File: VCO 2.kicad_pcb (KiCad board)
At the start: 2 copper layers, 182.4 x 128.6 mm, 0 parts

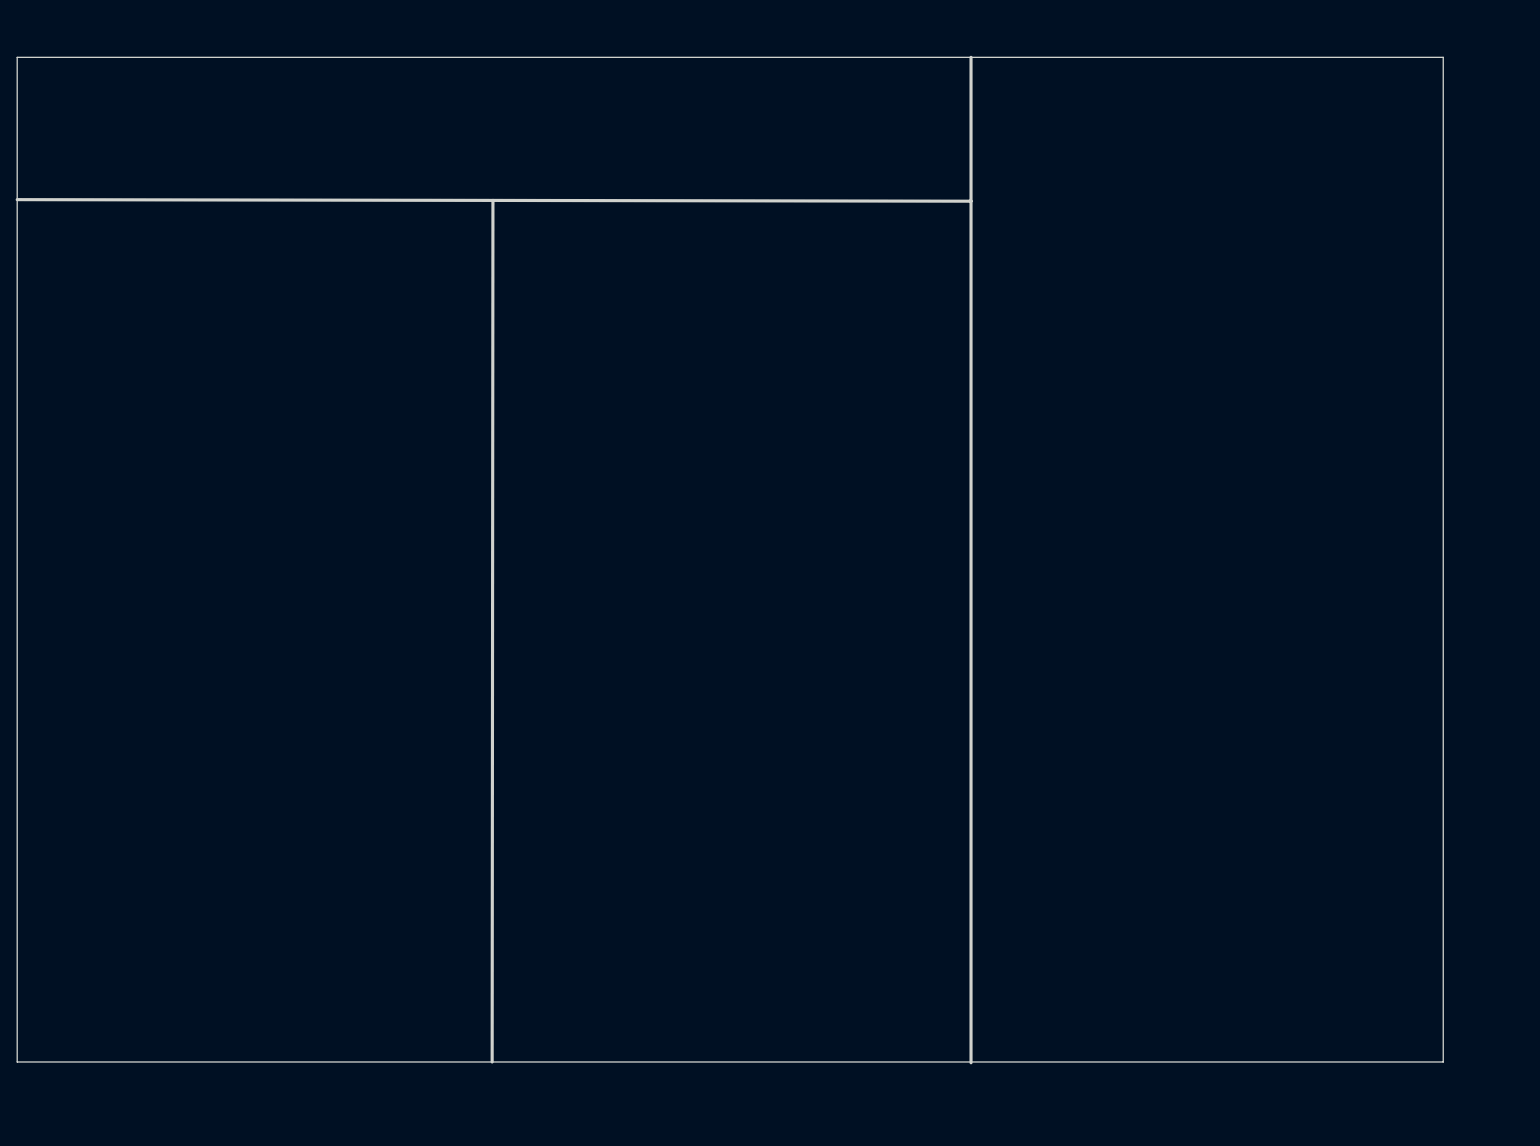
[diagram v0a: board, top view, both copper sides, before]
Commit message: Designed PCB and generated JLCPCB files
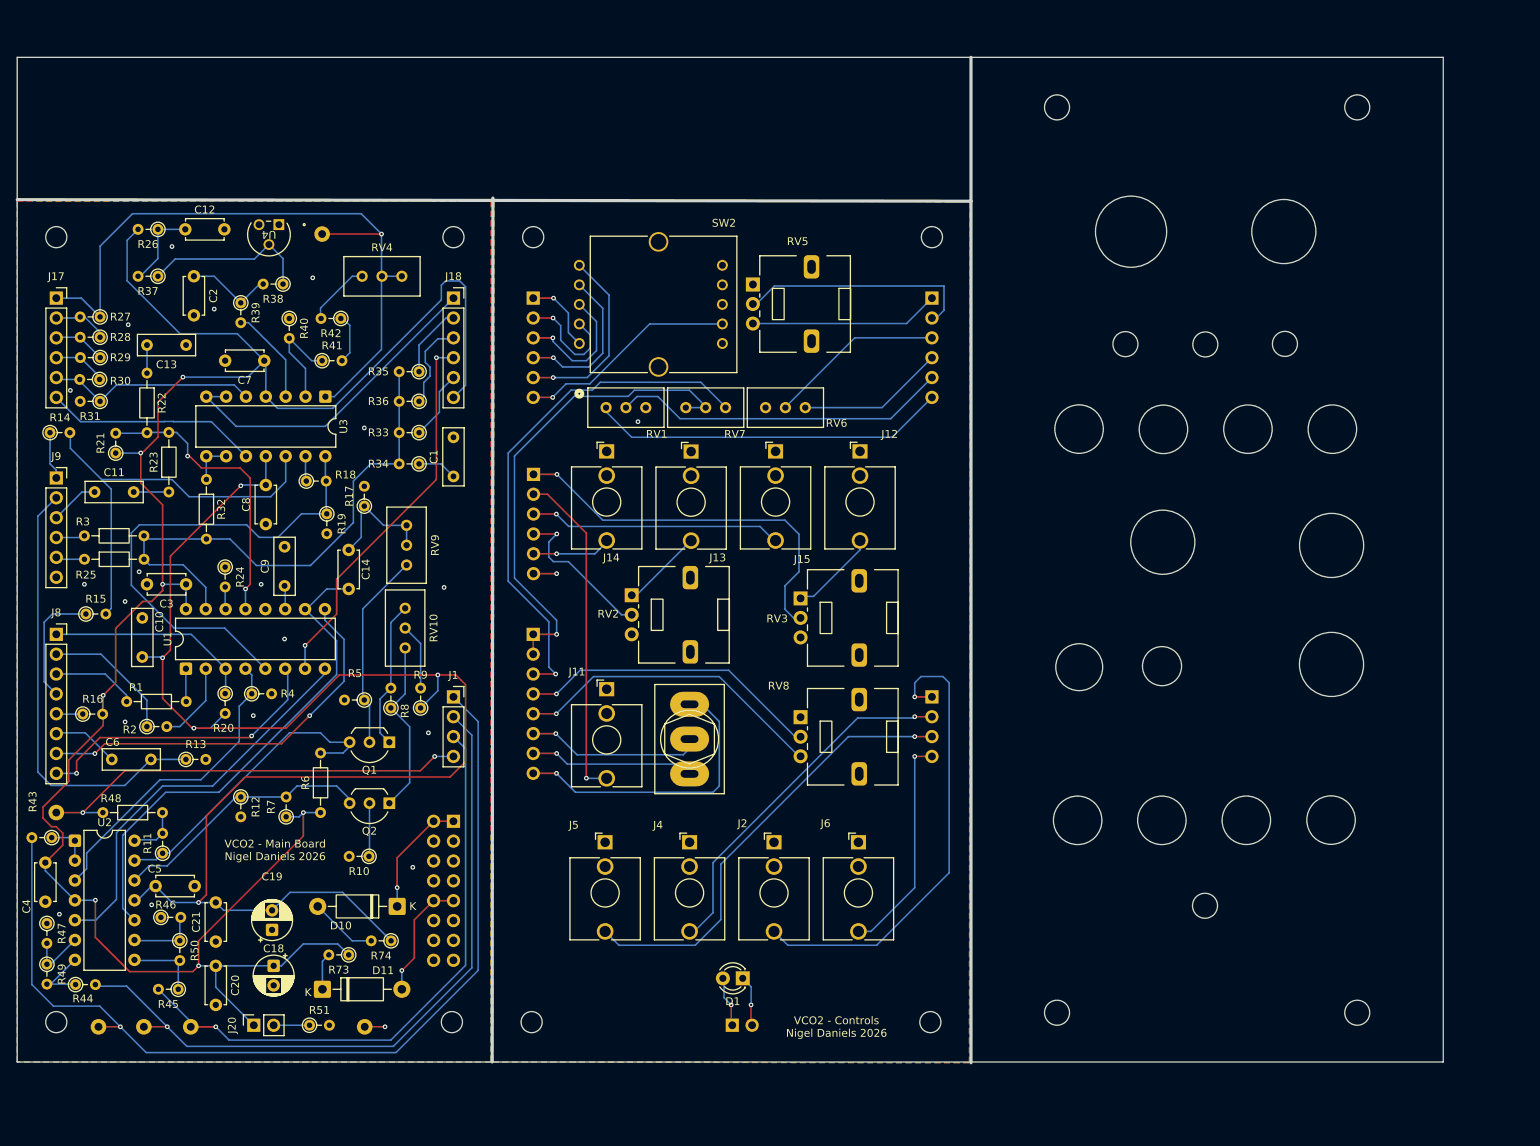
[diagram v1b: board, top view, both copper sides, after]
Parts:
- added C1: 10nF f, Capacitor_THT:C_Rect_L7.2mm_W2.5mm_P5.00mm, F.Cu at (75.8, 73.6)
- added C10: 100nF f, Capacitor_THT:C_Rect_L7.2mm_W2.5mm_P5.00mm, F.Cu at (36.0, 91.7)
- added C11: 100nF f, Capacitor_THT:C_Rect_L7.2mm_W2.5mm_P5.00mm, F.Cu at (29.9, 75.6)
- added C12: 0.1μF c, Capacitor_THT:C_Disc_D4.7mm_W2.5mm_P5.00mm, F.Cu at (41.5, 42.0)
- added C13: 1nF f, Capacitor_THT:C_Rect_L7.2mm_W2.5mm_P5.00mm, F.Cu at (41.6, 56.8)
- added C14: 10uF c, Capacitor_THT:C_Disc_D4.7mm_W2.5mm_P5.00mm, F.Cu at (62.4, 83.0)
- added C18: 47μF e, Capacitor_THT:CP_Radial_D5.0mm_P2.50mm, F.Cu at (52.8, 136.2)
- added C19: 47μF e, Capacitor_THT:CP_Radial_D5.0mm_P2.50mm, F.Cu at (52.6, 131.6)
- added C2: 10μF c, Capacitor_THT:C_Disc_D4.7mm_W2.5mm_P5.00mm, F.Cu at (42.6, 48.0)
- added C20: 0.1μF c, Capacitor_THT:C_Disc_D4.7mm_W2.5mm_P5.00mm, F.Cu at (45.4, 136.2)
- added C21: 0.1μF c, Capacitor_THT:C_Disc_D4.7mm_W2.5mm_P5.00mm, F.Cu at (45.4, 133.1)
- added C3: 100nF c, Capacitor_THT:C_Disc_D4.7mm_W2.5mm_P5.00mm, F.Cu at (41.6, 87.4)
- added C4: 0.1μF c, Capacitor_THT:C_Disc_D4.7mm_W2.5mm_P5.00mm, F.Cu at (23.6, 123.0)
- added C5: 0.1μF c, Capacitor_THT:C_Disc_D4.7mm_W2.5mm_P5.00mm, F.Cu at (42.7, 126.0)
- added C6: 1000pF f, Capacitor_THT:C_Rect_L7.2mm_W2.5mm_P5.00mm, F.Cu at (32.1, 109.8)
- added C7: 0.1μF c, Capacitor_THT:C_Disc_D4.7mm_W2.5mm_P5.00mm, F.Cu at (51.6, 58.8)
- added C8: 0.1μF c, Capacitor_THT:C_Disc_D4.7mm_W2.5mm_P5.00mm, F.Cu at (51.8, 79.7)
- added C9: 1nF f, Capacitor_THT:C_Rect_L7.2mm_W2.5mm_P5.00mm, F.Cu at (54.2, 87.6)
- added D1: LED, LED_THT:LED_D3.0mm_FlatTop, F.Cu at (112.8, 137.8)
- added D10: 1N5819, Diode_THT:D_DO-41_SOD81_P10.16mm_Horizontal, F.Cu at (68.6, 128.6)
- added D11: 1N5819, Diode_THT:D_DO-41_SOD81_P10.16mm_Horizontal, F.Cu at (59.0, 139.2)
- added H1: ~, MountingHole:MountingHole_2.7mm_M2.5, F.Cu at (25.0, 43.0)
- added H10: ~, MountingHole:MountingHole_3.2mm_M3, F.Cu at (191.4, 26.4)
- added H11: ~, MountingHole:MountingHole_3.2mm_M3, F.Cu at (191.4, 142.2)
- added H12: ~, MountingHole:MountingHole_3.2mm_M3, F.Cu at (153.0, 142.2)
- added H2: ~, MountingHole:MountingHole_2.7mm_M2.5, F.Cu at (75.8, 43.0)
- added H3: ~, MountingHole:MountingHole_2.7mm_M2.5, F.Cu at (25.0, 143.4)
- added H4: ~, MountingHole:MountingHole_2.7mm_M2.5, F.Cu at (75.6, 143.4)
- added H5: ~, MountingHole:MountingHole_2.7mm_M2.5, F.Cu at (86.0, 43.0)
- added H6: ~, MountingHole:MountingHole_2.7mm_M2.5, F.Cu at (137.0, 43.0)
- added H7: ~, MountingHole:MountingHole_2.7mm_M2.5, F.Cu at (136.8, 143.4)
- added H8: ~, MountingHole:MountingHole_2.7mm_M2.5, F.Cu at (85.8, 143.4)
- added H9: ~, MountingHole:MountingHole_3.2mm_M3, F.Cu at (153.0, 26.4)
- added J1: OUT 1x4s, Connector_PinSocket_2.54mm:PinSocket_1x04_P2.54mm_Vertical, F.Cu at (75.8, 101.8)
- added J10: IN 1x6h, Connector_PinHeader_2.54mm:PinHeader_1x06_P2.54mm_Vertical, B.Cu at (86.0, 73.3)
- added J11: SYNC, Connector_Audio:Jack_3.5mm_QingPu_WQP-PJ398SM_Vertical_CircularHoles, F.Cu at (95.4, 100.8)
- added J12: PWM, Connector_Audio:Jack_3.5mm_QingPu_WQP-PJ398SM_Vertical_CircularHoles, F.Cu at (127.8, 70.4)
- added J13: CV, Connector_Audio:Jack_3.5mm_QingPu_WQP-PJ398SM_Vertical_CircularHoles, F.Cu at (106.2, 70.4)
- added J14: 1VOct, Connector_Audio:Jack_3.5mm_QingPu_WQP-PJ398SM_Vertical_CircularHoles, F.Cu at (95.4, 70.4)
- added J15: FM, Connector_Audio:Jack_3.5mm_QingPu_WQP-PJ398SM_Vertical_CircularHoles, F.Cu at (117.0, 70.4)
- added J17: OCT 1x6s, Connector_PinSocket_2.54mm:PinSocket_1x06_P2.54mm_Vertical, F.Cu at (25.0, 50.8)
- added J18: CV 1x6s, Connector_PinSocket_2.54mm:PinSocket_1x06_P2.54mm_Vertical, F.Cu at (75.8, 50.8)
- added J19: CV 1x6h, Connector_PinHeader_2.54mm:PinHeader_1x06_P2.54mm_Vertical, B.Cu at (137.0, 50.8)
- added J2: SQR, Connector_Audio:Jack_3.5mm_QingPu_WQP-PJ398SM_Vertical_CircularHoles, F.Cu at (116.8, 120.4)
- added J20: LED 1x2s, Connector_PinSocket_2.54mm:PinSocket_1x02_P2.54mm_Vertical, F.Cu at (50.3, 143.8)
- added J21: LED 1x2h, Connector_PinHeader_2.54mm:PinHeader_1x02_P2.54mm_Vertical, B.Cu at (111.5, 143.8)
- added J22: OCT 1x6h, Connector_PinHeader_2.54mm:PinHeader_1x06_P2.54mm_Vertical, B.Cu at (86.0, 50.8)
- added J3: OUT 1x4h, Connector_PinHeader_2.54mm:PinHeader_1x04_P2.54mm_Vertical, B.Cu at (137.0, 101.8)
- added J4: SAW, Connector_Audio:Jack_3.5mm_QingPu_WQP-PJ398SM_Vertical_CircularHoles, F.Cu at (106.0, 120.4)
- added J5: TRI, Connector_Audio:Jack_3.5mm_QingPu_WQP-PJ398SM_Vertical_CircularHoles, F.Cu at (95.2, 120.4)
- added J6: SIN, Connector_Audio:Jack_3.5mm_QingPu_WQP-PJ398SM_Vertical_CircularHoles, F.Cu at (127.6, 120.4)
- added J7: CTRL 1x8h, Connector_PinHeader_2.54mm:PinHeader_1x08_P2.54mm_Vertical, B.Cu at (86.0, 93.8)
- added J8: CTRL 1x8s, Connector_PinSocket_2.54mm:PinSocket_1x08_P2.54mm_Vertical, F.Cu at (25.0, 93.8)
- added J85: Eurorack 2x8hs, Connector_PinHeader_2.54mm:PinHeader_2x08_P2.54mm_Vertical, B.Cu at (75.8, 117.7)
- added J9: IN 1x6s, Connector_PinSocket_2.54mm:PinSocket_1x06_P2.54mm_Vertical, F.Cu at (25.0, 73.8)
- added Q1: 2N3904, Package_TO_SOT_THT:TO-92_Inline_Wide, F.Cu at (67.6, 107.6)
- added Q2: 2N3904, Package_TO_SOT_THT:TO-92_Inline_Wide, F.Cu at (67.6, 115.4)
- added R1: 24K, Resistor_THT:R_Axial_DIN0204_L3.6mm_D1.6mm_P7.62mm_Horizontal, F.Cu at (34.0, 102.4)
- added R10: 470R, Resistor_THT:R_Axial_DIN0204_L3.6mm_D1.6mm_P2.54mm_Vertical, F.Cu at (65.0, 122.2)
- added R11: 33K, Resistor_THT:R_Axial_DIN0204_L3.6mm_D1.6mm_P2.54mm_Vertical, F.Cu at (38.6, 121.8)
- added R12: 33K, Resistor_THT:R_Axial_DIN0204_L3.6mm_D1.6mm_P2.54mm_Vertical, F.Cu at (48.6, 114.6)
- added R13: 100K, Resistor_THT:R_Axial_DIN0204_L3.6mm_D1.6mm_P2.54mm_Vertical, F.Cu at (41.6, 109.8)
- added R14: 100K, Resistor_THT:R_Axial_DIN0204_L3.6mm_D1.6mm_P2.54mm_Vertical, F.Cu at (24.2, 68.0)
- added R15: 100K, Resistor_THT:R_Axial_DIN0204_L3.6mm_D1.6mm_P2.54mm_Vertical, F.Cu at (28.8, 91.2)
- added R16: 100K, Resistor_THT:R_Axial_DIN0204_L3.6mm_D1.6mm_P2.54mm_Vertical, F.Cu at (28.4, 104.0)
- added R17: 10K, Resistor_THT:R_Axial_DIN0204_L3.6mm_D1.6mm_P2.54mm_Vertical, F.Cu at (64.4, 77.4)
- added R18: 100K, Resistor_THT:R_Axial_DIN0204_L3.6mm_D1.6mm_P2.54mm_Vertical, F.Cu at (57.0, 74.2)
- added R19: 4K7, Resistor_THT:R_Axial_DIN0204_L3.6mm_D1.6mm_P2.54mm_Vertical, F.Cu at (59.6, 78.4)
- added R2: 5K6, Resistor_THT:R_Axial_DIN0204_L3.6mm_D1.6mm_P2.54mm_Vertical, F.Cu at (36.6, 105.6)
- added R20: 680R, Resistor_THT:R_Axial_DIN0204_L3.6mm_D1.6mm_P2.54mm_Vertical, F.Cu at (46.6, 101.4)
- added R21: 1M2, Resistor_THT:R_Axial_DIN0204_L3.6mm_D1.6mm_P2.54mm_Vertical, F.Cu at (32.6, 70.6)
- added R22: 470R, Resistor_THT:R_Axial_DIN0204_L3.6mm_D1.6mm_P7.62mm_Horizontal, F.Cu at (36.6, 60.4)
- added R23: 1M, Resistor_THT:R_Axial_DIN0204_L3.6mm_D1.6mm_P7.62mm_Horizontal, F.Cu at (39.4, 75.6)
- added R24: P1K8, Resistor_THT:R_Axial_DIN0204_L3.6mm_D1.6mm_P2.54mm_Vertical, F.Cu at (46.6, 85.2)
- added R25: 100K, Resistor_THT:R_Axial_DIN0204_L3.6mm_D1.6mm_P7.62mm_Horizontal, F.Cu at (28.6, 84.2)
- added R26: 4K7, Resistor_THT:R_Axial_DIN0204_L3.6mm_D1.6mm_P2.54mm_Vertical, F.Cu at (38.0, 42.0)
- added R27: P10K, Resistor_THT:R_Axial_DIN0204_L3.6mm_D1.6mm_P2.54mm_Vertical, F.Cu at (30.6, 53.2)
- added R28: P10K, Resistor_THT:R_Axial_DIN0204_L3.6mm_D1.6mm_P2.54mm_Vertical, F.Cu at (30.6, 55.8)
- added R29: P10K, Resistor_THT:R_Axial_DIN0204_L3.6mm_D1.6mm_P2.54mm_Vertical, F.Cu at (30.6, 58.4)
- added R3: 470K, Resistor_THT:R_Axial_DIN0204_L3.6mm_D1.6mm_P7.62mm_Horizontal, F.Cu at (28.6, 81.2)
- added R30: P10K, Resistor_THT:R_Axial_DIN0204_L3.6mm_D1.6mm_P2.54mm_Vertical, F.Cu at (30.5, 61.2)
- added R31: P10K, Resistor_THT:R_Axial_DIN0204_L3.6mm_D1.6mm_P2.54mm_Vertical, F.Cu at (30.6, 64.0)
- added R32: 100K, Resistor_THT:R_Axial_DIN0204_L3.6mm_D1.6mm_P7.62mm_Horizontal, F.Cu at (44.2, 74.0)
- added R33: 100K, Resistor_THT:R_Axial_DIN0204_L3.6mm_D1.6mm_P2.54mm_Vertical, F.Cu at (71.4, 68.0)
- added R34: 470R, Resistor_THT:R_Axial_DIN0204_L3.6mm_D1.6mm_P2.54mm_Vertical, F.Cu at (71.4, 72.0)
- added R35: 100K, Resistor_THT:R_Axial_DIN0204_L3.6mm_D1.6mm_P2.54mm_Vertical, F.Cu at (71.4, 60.2)
- added R36: 1M, Resistor_THT:R_Axial_DIN0204_L3.6mm_D1.6mm_P2.54mm_Vertical, F.Cu at (71.4, 64.0)
- added R37: 4K7, Resistor_THT:R_Axial_DIN0204_L3.6mm_D1.6mm_P2.54mm_Vertical, F.Cu at (38.0, 48.0)
- added R38: 33K, Resistor_THT:R_Axial_DIN0204_L3.6mm_D1.6mm_P2.54mm_Vertical, F.Cu at (54.0, 49.0)
- added R39: 33K, Resistor_THT:R_Axial_DIN0204_L3.6mm_D1.6mm_P2.54mm_Vertical, F.Cu at (48.6, 51.4)
- added R4: 10K, Resistor_THT:R_Axial_DIN0204_L3.6mm_D1.6mm_P2.54mm_Vertical, F.Cu at (50.0, 101.4)
- added R40: 10K, Resistor_THT:R_Axial_DIN0204_L3.6mm_D1.6mm_P2.54mm_Vertical, F.Cu at (54.8, 53.4)
- added R41: 9.1K, Resistor_THT:R_Axial_DIN0204_L3.6mm_D1.6mm_P2.54mm_Vertical, F.Cu at (59.0, 58.8)
- added R42: 510R, Resistor_THT:R_Axial_DIN0204_L3.6mm_D1.6mm_P2.54mm_Vertical, F.Cu at (61.4, 53.4)
- added R43: 1K, Resistor_THT:R_Axial_DIN0204_L3.6mm_D1.6mm_P2.54mm_Vertical, F.Cu at (24.4, 119.8)
- added R44: 1K, Resistor_THT:R_Axial_DIN0204_L3.6mm_D1.6mm_P2.54mm_Vertical, F.Cu at (27.5, 138.6)
- added R45: 1K, Resistor_THT:R_Axial_DIN0204_L3.6mm_D1.6mm_P2.54mm_Vertical, F.Cu at (40.6, 139.2)
- added R46: 1K, Resistor_THT:R_Axial_DIN0204_L3.6mm_D1.6mm_P2.54mm_Vertical, F.Cu at (38.4, 130.0)
- added R47: 1K, Resistor_THT:R_Axial_DIN0204_L3.6mm_D1.6mm_P2.54mm_Vertical, F.Cu at (23.8, 130.8)
- added R48: 1K, Resistor_THT:R_Axial_DIN0204_L3.6mm_D1.6mm_P7.62mm_Horizontal, F.Cu at (38.6, 116.6)
- added R49: 220R, Resistor_THT:R_Axial_DIN0204_L3.6mm_D1.6mm_P2.54mm_Vertical, F.Cu at (23.8, 136.0)
- added R5: 470R, Resistor_THT:R_Axial_DIN0204_L3.6mm_D1.6mm_P2.54mm_Vertical, F.Cu at (64.4, 102.2)
- added R50: 1K5, Resistor_THT:R_Axial_DIN0204_L3.6mm_D1.6mm_P2.54mm_Vertical, F.Cu at (40.8, 133.0)
- added R51: 470R/520R, Resistor_THT:R_Axial_DIN0204_L3.6mm_D1.6mm_P2.54mm_Vertical, F.Cu at (57.4, 143.8)
- added R6: 10K, Resistor_THT:R_Axial_DIN0204_L3.6mm_D1.6mm_P7.62mm_Horizontal, F.Cu at (58.8, 116.6)
- added R7: 10K, Resistor_THT:R_Axial_DIN0204_L3.6mm_D1.6mm_P2.54mm_Vertical, F.Cu at (54.4, 117.1)
- added R73: 10R, Resistor_THT:R_Axial_DIN0204_L3.6mm_D1.6mm_P2.54mm_Vertical, F.Cu at (62.4, 134.8)
- added R74: 10R, Resistor_THT:R_Axial_DIN0204_L3.6mm_D1.6mm_P2.54mm_Vertical, F.Cu at (67.8, 133.0)
- added R8: 220, Resistor_THT:R_Axial_DIN0204_L3.6mm_D1.6mm_P2.54mm_Vertical, F.Cu at (67.8, 103.2)
- added R9: 68K, Resistor_THT:R_Axial_DIN0204_L3.6mm_D1.6mm_P2.54mm_Vertical, F.Cu at (71.6, 103.2)
- added RV1: CNTR 100K, Potentiometer_THT:Potentiometer_Bourns_3296W_Vertical, F.Cu at (100.4, 64.8)
- added RV10: OFFSET 50k, Potentiometer_THT:Potentiometer_Bourns_3296W_Vertical, F.Cu at (69.6, 95.5)
- added RV2: CV_LVL 100K, Potentiometer_THT:Potentiometer_Alps_RK09L_Single_Vertical, F.Cu at (98.6, 88.8)
- added RV3: PWM_LVL 100K, Potentiometer_THT:Potentiometer_Alps_RK09L_Single_Vertical, F.Cu at (120.2, 89.2)
- added RV4: REF 1K, Potentiometer_THT:Potentiometer_Bourns_3296W_Vertical, F.Cu at (69.2, 48.0)
- added RV5: FINE 100K, Potentiometer_THT:Potentiometer_Alps_RK09L_Single_Vertical, F.Cu at (114.1, 49.0)
- added RV6: HF_TRK 20K, Potentiometer_THT:Potentiometer_Bourns_3296W_Vertical, F.Cu at (120.8, 64.8)
- added RV7: TRK 10K, Potentiometer_THT:Potentiometer_Bourns_3296W_Vertical, F.Cu at (110.6, 64.8)
- added RV8: PW 100K, Potentiometer_THT:Potentiometer_Alps_RK09L_Single_Vertical, F.Cu at (120.2, 104.4)
- added RV9: RND 100k, Potentiometer_THT:Potentiometer_Bourns_3296W_Vertical, F.Cu at (69.8, 84.9)
- added SW1: SW_SPDT, Switch:SW_Toggle_Blue_wSlots, F.Cu at (106.0, 107.2)
- added SW2: SW_Rotary_1x6_MP, Rotary Switch:SR1712F-0106-20F0A-N9-N-027_ATW, F.Cu at (91.9, 56.6)
- added TP1: +5V Ref, TestPoint:TestPoint_Loop_D2.50mm_Drill1.0mm, B.Cu at (59.0, 42.6)
- added TP2: Sqr, TestPoint:TestPoint_Loop_D2.50mm_Drill1.0mm, B.Cu at (30.4, 144.0)
- added TP22: Gnd, TestPoint:TestPoint_Loop_D2.50mm_Drill1.0mm, B.Cu at (64.5, 144.0)
- added TP3: Saw, TestPoint:TestPoint_Loop_D2.50mm_Drill1.0mm, B.Cu at (36.2, 144.0)
- added TP4: Tri, TestPoint:TestPoint_Loop_D2.50mm_Drill1.0mm, B.Cu at (42.2, 144.0)
- added TP5: Sine, TestPoint:TestPoint_Loop_D2.50mm_Drill1.0mm, B.Cu at (25.0, 116.6)
- added U1: CEM3340, Package_DIP:DIP-16_W7.62mm, F.Cu at (41.6, 98.2)
- added U2: TL074, Package_DIP:DIP-14_W7.62mm, F.Cu at (27.4, 120.2)
- added U3: TL074, Package_DIP:DIP-14_W7.62mm, F.Cu at (59.4, 63.4)
- added U4: LM336Z-2.5, Voltage Ref Diode:Z03A, F.Cu at (53.5, 41.4)
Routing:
- net +12V: track 0.00 -> 286.1 mm, vias 0 -> 8
- net -12V: track 0.00 -> 205.6 mm, vias 0 -> 6
- net SQR: track 0.00 -> 122.5 mm, vias 0 -> 1
- net SAW: track 0.00 -> 91.7 mm, vias 0 -> 1
- net REF: track 0.00 -> 89.5 mm, vias 0 -> 1
- net TRI: track 0.00 -> 79.0 mm, vias 0 -> 1
- net CV: track 0.00 -> 69.8 mm
- net Net-(J7-Pin_3): track 0.00 -> 66.6 mm, vias 0 -> 1
- net SIN: track 0.00 -> 64.0 mm
- net PWM: track 0.00 -> 63.0 mm
- net Net-(J7-Pin_1): track 0.00 -> 62.1 mm, vias 0 -> 1
- net Net-(J3-Pin_1): track 0.00 -> 60.3 mm, vias 0 -> 1
- net Net-(J3-Pin_3): track 0.00 -> 57.7 mm, vias 0 -> 1
- net Net-(J9-Pin_2): track 0.00 -> 57.1 mm
- net Net-(J1-Pin_4): track 0.00 -> 57.0 mm, vias 0 -> 2
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- added copper zone on B.Cu, net GND
- added copper zone on F.Cu, net GND
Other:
- outline, holes or cut-outs redrawn
- board text added: "VCO2 - Controls Nigel Daniels 2026"
- board text added: "VCO2 - Main Board Nigel Daniels 2026"
- board text added: "VCO2 PCB Design"

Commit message: Panelized design using tab and mouse bites
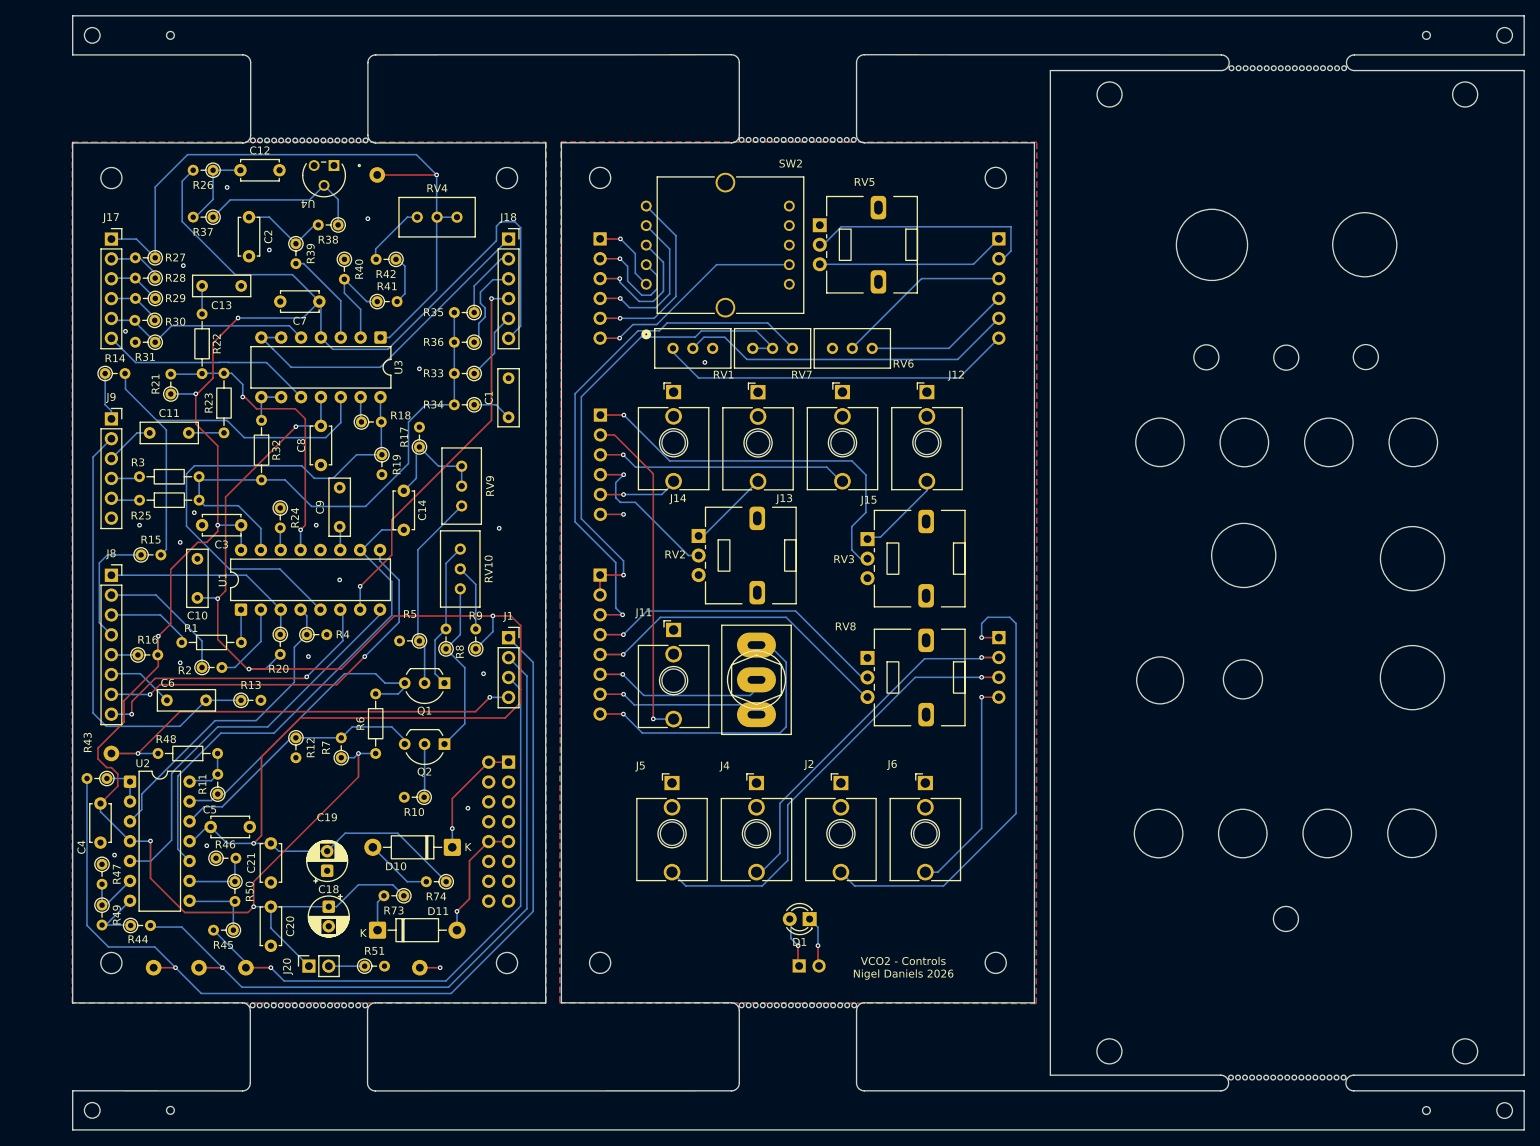
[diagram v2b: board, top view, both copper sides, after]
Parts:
- moved H11 14.7 mm to (205.2, 147.1)
- moved H10 13.9 mm to (205.2, 24.8)
- moved H8 11.6 mm to (94.6, 135.8)
- moved J21 11.4 mm to (120.0, 136.2)
- moved J6 11.4 mm to (136.2, 112.8)
- moved J19 11.4 mm to (145.6, 43.2)
- moved J3 11.4 mm to (145.6, 94.2)
- moved D1 11.4 mm to (121.4, 130.2)
- moved J10 11.4 mm to (94.6, 65.8)
- moved J12 11.4 mm to (136.4, 62.8)
- moved J14 11.4 mm to (104.0, 62.8)
- moved J15 11.4 mm to (125.6, 62.8)
- moved J2 11.4 mm to (125.4, 112.8)
- moved J4 11.4 mm to (114.6, 112.8)
- moved J5 11.4 mm to (103.8, 112.8)
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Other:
- board size 182.4 x 128.6 mm -> 185.7 x 142.5 mm
- board text added: "VCO2 - Front Panel Nigel Daniels 2026"
- board text removed: "v-cut line (horizontal)"
- board text removed: "v-cut line (vertical)"
